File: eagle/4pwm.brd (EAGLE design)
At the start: 16.5 x 15.2 mm, 17 parts, among them U1 Tiny85-20-SMT

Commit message: Did some manual routing on the breakout
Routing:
- net N$7: track 24.6 -> 14.5 mm
- net VCC: track 41.2 -> 45.9 mm
- net N$5: track 19.9 -> 17.5 mm
- net N$4: track 14.6 -> 12.5 mm
- net GND: track 28.8 -> 27.0 mm, vias 3 -> 2
- net N$3: track 3.51 -> 4.90 mm
- net N$1: track 5.30 -> 4.43 mm

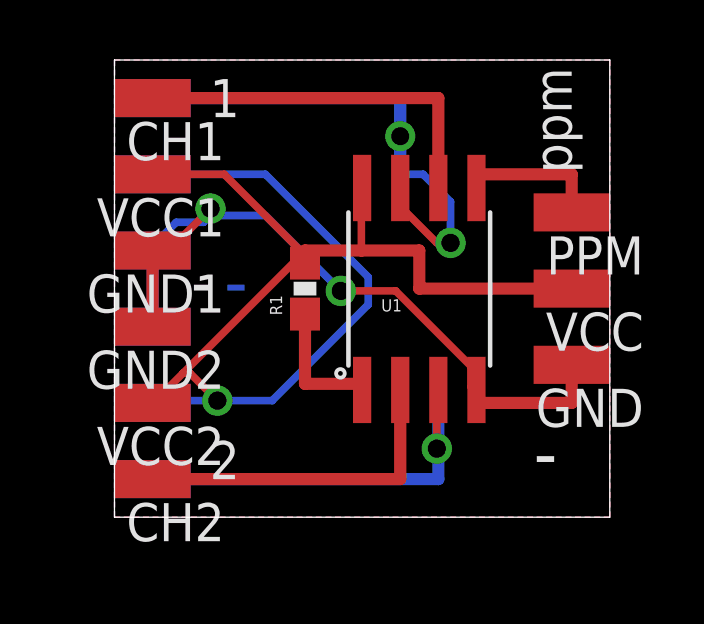
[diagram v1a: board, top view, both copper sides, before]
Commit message: Fixed up the labels to match reality
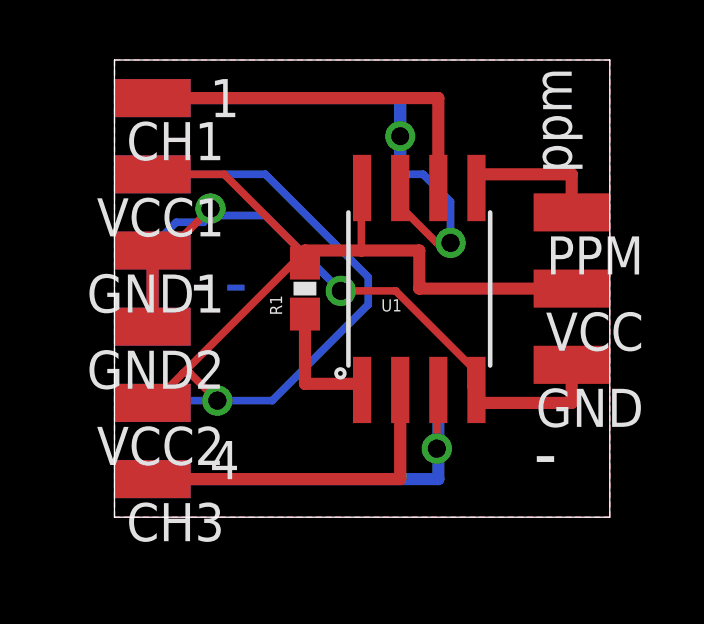
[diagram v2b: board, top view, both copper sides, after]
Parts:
- moved CH2 12.7 mm to (1.27, 14.0), flipped to the bottom
- moved CH3 12.7 mm to (1.27, 1.27), flipped to the top
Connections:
- net N$5: now also CH2.1; no longer CH3.1
- net N$6: now also CH3.1; no longer CH2.1
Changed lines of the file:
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@@
 <text x="2.54" y="6.985" size="1.778" layer="21" font="fixed">-</text>
 <text x="3.175" y="13.335" size="1.27" layer="21" font="fixed">1</text>
-<text x="3.175" y="1.27" size="1.27" layer="21" font="fixed">2</text>
-<text x="4.445" y="13.335" size="1.27" layer="22" font="fixed" rot="MR0">3</text>
-<text x="4.445" y="1.27" size="1.27" layer="22" font="fixed" rot="MR0">4</text>
+<text x="3.175" y="1.27" size="1.27" layer="21" font="fixed">4</text>
+<text x="4.445" y="13.335" size="1.27" layer="22" font="fixed" rot="MR0">2</text>
+<text x="4.445" y="1.27" size="1.27" layer="22" font="fixed" rot="MR0">3</text>
 <text x="4.445" y="6.985" size="1.778" layer="16" font="fixed" rot="MR0">-</text>
 <text x="3.81" y="6.985" size="1.778" layer="22" font="fixed" rot="MR0">-</text>
@@
 <elements>
 <element name="CH1" library="wirepad" package="SMD1,27-2,54" value="" x="1.27" y="13.97" rot="R90"/>
-<element name="CH2" library="wirepad" package="SMD1,27-2,54" value="" x="1.27" y="1.27" rot="R90"/>
-<element name="CH3" library="wirepad" package="SMD1,27-2,54" value="" x="1.27" y="13.97" rot="MR90"/>
+<element name="CH3" library="wirepad" package="SMD1,27-2,54" value="" x="1.27" y="1.27" rot="R90"/>
+<element name="CH2" library="wirepad" package="SMD1,27-2,54" value="" x="1.27" y="13.97" rot="MR90"/>
 <element name="CH4" library="wirepad" package="SMD1,27-2,54" value="" x="1.27" y="1.27" rot="MR90"/>
 <element name="GND" library="wirepad" package="SMD1,27-2,54" value="" x="15.24" y="5.08" rot="R90"/>
@@
 <signal name="N$5">
 <contactref element="U1" pad="7"/>
-<contactref element="CH3" pad="1"/>
+<contactref element="CH2" pad="1"/>
 <wire x1="1.27" y1="13.97" x2="9.525" y2="13.97" width="0.4064" layer="16"/>
 <wire x1="9.525" y1="13.97" x2="9.525" y2="11.43" width="0.4064" layer="16"/>
@@
 <signal name="N$6">
 <contactref element="U1" pad="2"/>
-<contactref element="CH2" pad="1"/>
+<contactref element="CH3" pad="1"/>
 <wire x1="9.525" y1="4.2418" x2="9.525" y2="1.27" width="0.4064" layer="1"/>
 <wire x1="9.525" y1="1.27" x2="1.27" y2="1.27" width="0.4064" layer="1"/>

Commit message: Remove unnecessary reset pullup
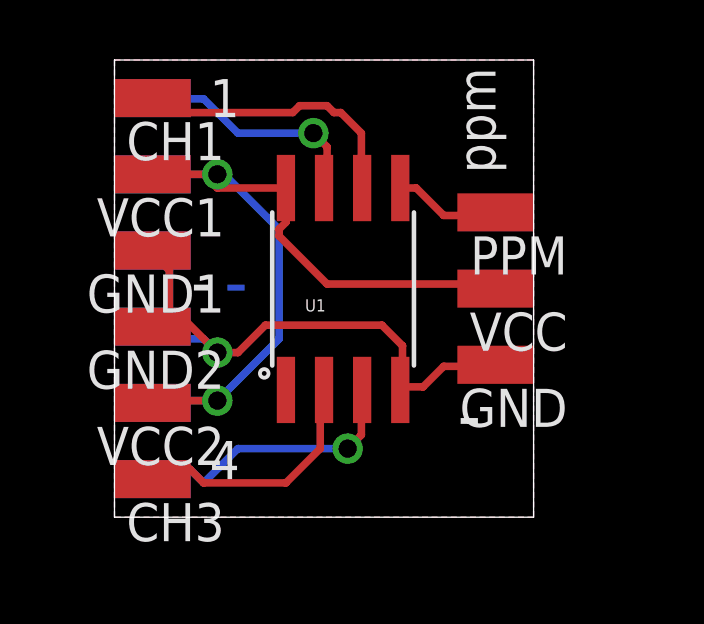
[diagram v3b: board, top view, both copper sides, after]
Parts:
- removed R1: 10K, SparkFun-Passives:0603-RES
- moved GND 2.54 mm to (12.7, 5.08)
- moved PPM 2.54 mm to (12.7, 10.2)
- moved VCC 2.54 mm to (12.7, 7.62)
- moved U1 2.54 mm to (7.62, 7.62)
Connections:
- removed net N$1: R1.1, U1.1
- net VCC: no longer R1.2
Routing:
- net VCC: track 45.9 -> 30.5 mm, vias 1 -> 2
- net N$5: track 17.5 -> 7.96 mm
- net N$7: track 14.5 -> 9.45 mm
- net N$1: track 4.43 -> 0.00 mm
- net GND: track 27.0 -> 23.0 mm, vias 2 -> 1
- net N$4: track 12.5 -> 9.48 mm
- net N$6: track 11.2 -> 8.40 mm
- net N$3: track 4.90 -> 3.59 mm
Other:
- board size 16.5 x 15.2 mm -> 14 x 15.2 mm
